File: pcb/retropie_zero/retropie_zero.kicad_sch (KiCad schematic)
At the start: 32 parts, among them J1 Conn_01x02_Socket, J2 Conn_01x10_Pin, SW1 SW_DIP_x01, SW10 SW_DIP_x01, SW11 SW_DIP_x01, SW12 SW_DIP_x01, SW13 SW_DIP_x01, SW14 SW_DIP_x01, SW2 SW_DIP_x01, SW3 SW_DIP_x01, SW4 SW_DIP_x01, SW5 SW_DIP_x01, SW6 SW_DIP_x01, SW7 SW_DIP_x01, SW8 SW_DIP_x01, SW9 SW_DIP_x01, U3 PAM8302AASCR, X1 TERMBLOCK_1X2

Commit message: Fixed some stuff, removed irrelevant reference
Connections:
- net DPAD_D: now also U1.5 (GPIO3)
- net DPAD_L: now also U1.7 (GPIO4)
- net DPAD_R: now also U1.11 (GPIO17)
- net DPAD_U: now also U1.3 (GPIO2)
- net L_BUMP: now also U1.8 (GPIO14)
- net R_BUMP: now also U1.16 (GPIO23)
- net R_TRIG: now also U1.10 (GPIO15), U1.26 (GPIO7)
- net SW_A: now also U1.29 (GPIO5)
- net SW_B: now also U1.15 (GPIO22)
- net SW_SEL: now also U1.31 (GPIO6)
- net SW_STA: now also U1.35 (GPIO19)
- net SW_X: now also U1.13 (GPIO27)
- net SW_Y: now also U1.21 (GPIO9)

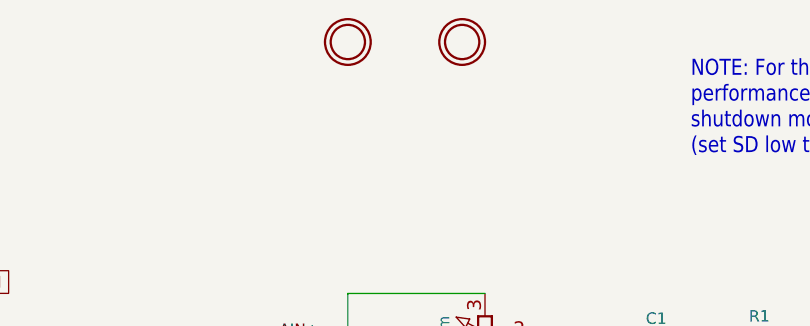
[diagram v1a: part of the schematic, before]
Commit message: Assigned footprints, ignoring backups now
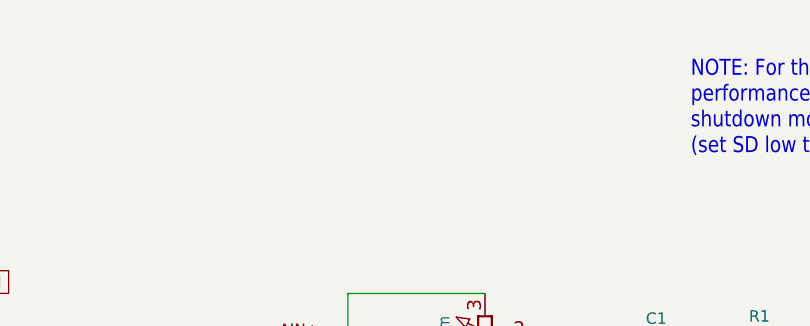
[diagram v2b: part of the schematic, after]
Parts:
- removed U$10, U$11: MOUNTINGHOLE2.0, Adafruit PAM8302:MOUNTINGHOLE_2.0_PLATED, symbol Adafruit PAM8302-eagle-import:MOUNTINGHOLE2.0
- C1, C2, C3, C4, C5: footprint Adafruit PAM8302:0805-NO -> Capacitor_SMD:C_0805_2012Metric_Pad1.18x1.45mm_HandSolder
- FB1, FB2: footprint Adafruit PAM8302:_0805 -> Capacitor_SMD:C_0805_2012Metric
- J1: footprint (none) -> Connector_PinHeader_2.54mm:PinHeader_1x02_P2.54mm_Vertical
- J2: footprint (none) -> Connector_PinHeader_2.54mm:PinHeader_1x10_P2.54mm_Vertical
- R1, R2, R3: footprint Adafruit PAM8302:0805-NO -> Resistor_SMD:R_0805_2012Metric
- SW1, SW10, SW11, SW12, SW13, SW14, SW2, SW3, SW4, SW5, SW6, SW7, SW8, SW9: footprint (none) -> Button_Switch_THT:SW_PUSH_6mm
- U1: footprint (none) -> lib:RPI Zero Footprint
- U3: footprint Adafruit PAM8302:MSOP8_0.65MM -> lib:PAM8302AADCR
- VR1: footprint Adafruit PAM8302:TRIMPOT_BOURNS_3303W -> Potentiometer_THT:Potentiometer_Runtron_RM-065_Vertical
- X1: footprint Adafruit PAM8302:TERMBLOCK_1X2-3.5MM -> TerminalBlock_4Ucon:TerminalBlock_4Ucon_1x02_P3.50mm_Horizontal
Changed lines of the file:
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@@
 			)
 		)
-		(property "Footprint" "Adafruit PAM8302:0805-NO"
+		(property "Footprint" "Capacitor_SMD:C_0805_2012Metric_Pad1.18x1.45mm_HandSolder"
 			(at 241.3 68.58 0)
 			(effects
@@
 			)
 		)
-		(property "Footprint" "Adafruit PAM8302:_0805"
+		(property "Footprint" "Capacitor_SMD:C_0805_2012Metric"
 			(at 228.6 50.8 0)
 			(effects
@@
 			)
 		)
-		(property "Footprint" "Adafruit PAM8302:MSOP8_0.65MM"
+		(property "Footprint" "lib:PAM8302AADCR"
 			(at 210.82 60.96 0)
 			(effects
@@
 			)
 		)
-		(property "Footprint" ""
+		(property "Footprint" "Button_Switch_THT:SW_PUSH_6mm"
 			(at 161.29 152.4 0)
 			(effects
@@
 			)
 		)
-		(property "Footprint" ""
+		(property "Footprint" "Button_Switch_THT:SW_PUSH_6mm"
 			(at 81.28 194.31 0)
 			(effects
@@
 			)
 		)
-		(property "Footprint" "Adafruit PAM8302:0805-NO"
+		(property "Footprint" "Capacitor_SMD:C_0805_2012Metric_Pad1.18x1.45mm_HandSolder"
 			(at 180.34 78.74 0)
 			(effects
@@
 			)
 		)
-		(property "Footprint" ""
+		(property "Footprint" "lib:RPI Zero Footprint"
 			(at 58.42 53.34 0)
 			(effects
@@
 			)
 		)
-		(property "Footprint" ""
+		(property "Footprint" "Connector_PinHeader_2.54mm:PinHeader_1x02_P2.54mm_Vertical"
 			(at 127 60.96 0)
 			(effects
@@
 	)
 	(symbol
-		(lib_id "Adafruit PAM8302-eagle-import:MOUNTINGHOLE2.0")
-		(at 144.78 17.78 0)
-		(unit 1)
-		(exclude_from_sim no)
-		(in_bom yes)
-		(on_board yes)
-		(dnp no)
-		(property "Reference" "U$11"
-			(at 144.78 17.78 0)
-			(effects
-				(font
-					(size 1.27 1.27)
-				)
-				(hide yes)
-			)
-		)
-		(property "Value" "MOUNTINGHOLE2.0"
-			(at 144.78 17.78 0)
-			(effects
-				(font
-					(size 1.27 1.27)
-				)
-				(hide yes)
-			)
-		)
-		(property "Footprint" "Adafruit PAM8302:MOUNTINGHOLE_2.0_PLATED"
-			(at 144.78 17.78 0)
-			(effects
-				(font
-					(size 1.27 1.27)
-				)
-				(hide yes)
-			)
-		)
-		(property "Datasheet" ""
-			(at 144.78 17.78 0)
-			(effects
-				(font
-					(size 1.27 1.27)
-				)
-				(hide yes)
-			)
-		)
-		(property "Description" ""
-			(at 144.78 17.78 0)
-			(effects
-				(font
-					(size 1.27 1.27)
-				)
-				(hide yes)
-			)
-		)
-		(instances
-			(project "retropie_zero"
-				(path "/f5395351-1217-49d5-a52e-3316d9db527f"
-					(reference "U$11")
-					(unit 1)
-				)
-			)
-		)
-	)
-	(symbol
 		(lib_id "Switch:SW_DIP_x01")
 		(at 181.61 152.4 0)
@@
 			)
 		)
-		(property "Footprint" ""
+		(property "Footprint" "Button_Switch_THT:SW_PUSH_6mm"
 			(at 181.61 152.4 0)
 			(effects
@@
 			)
 		)
-		(property "Footprint" "Adafruit PAM8302:0805-NO"
+		(property "Footprint" "Capacitor_SMD:C_0805_2012Metric_Pad1.18x1.45mm_HandSolder"
 			(at 177.8 50.8 0)
 			(effects
@@
 			)
 		)
-		(property "Footprint" ""
+		(property "Footprint" "Button_Switch_THT:SW_PUSH_6mm"
 			(at 194.31 195.58 0)
 			(effects
@@
 			)
 		)
-		(property "Footprint" ""
+		(property "Footprint" "Button_Switch_THT:SW_PUSH_6mm"
 			(at 148.59 195.58 0)
 			(effects
@@
 			)
 		)
-		(property "Footprint" ""
+		(property "Footprint" "Button_Switch_THT:SW_PUSH_6mm"
 			(at 77.47 152.4 0)
 			(effects
@@
 			)
 		)
-		(property "Footprint" "Adafruit PAM8302:TERMBLOCK_1X2-3.5MM"
+		(property "Footprint" "TerminalBlock_4Ucon:TerminalBlock_4Ucon_1x02_P3.50mm_Horizontal"
 			(at 261.62 55.88 0)
 			(effects
@@
 			)
 		)
-		(property "Footprint" ""
+		(property "Footprint" "Button_Switch_THT:SW_PUSH_6mm"
 			(at 57.15 214.63 0)
 			(effects
@@
 			)
 		)
-		(property "Footprint" "Adafruit PAM8302:0805-NO"
+		(property "Footprint" "Capacitor_SMD:C_0805_2012Metric_Pad1.18x1.45mm_HandSolder"
 			(at 233.68 68.58 0)
 			(effects
@@
 			)
 		)
-		(property "Footprint" ""
+		(property "Footprint" "Button_Switch_THT:SW_PUSH_6mm"
 			(at 170.18 181.61 0)
 			(effects
@@
 			)
 		)
-		(property "Footprint" "Adafruit PAM8302:0805-NO"
+		(property "Footprint" "Resistor_SMD:R_0805_2012Metric"
 			(at 190.5 60.96 0)
 			(effects
@@
 			)
 		)
-		(property "Footprint" ""
+		(property "Footprint" "Button_Switch_THT:SW_PUSH_6mm"
 			(at 35.56 194.31 0)
 			(effects
@@
 			)
 		)
-		(property "Footprint" "Adafruit PAM8302:0805-NO"
+		(property "Footprint" "Capacitor_SMD:C_0805_2012Metric_Pad1.18x1.45mm_HandSolder"
 			(at 177.8 60.96 0)
 			(effects
@@
 			)
 		)
-		(property "Footprint" ""
+		(property "Footprint" "Button_Switch_THT:SW_PUSH_6mm"
 			(at 102.87 222.25 0)
 			(effects
@@
 			)
 		)
-		(property "Footprint" ""
+		(property "Footprint" "Button_Switch_THT:SW_PUSH_6mm"
 			(at 57.15 152.4 0)
 			(effects
@@
 			)
 		)
-		(property "Footprint" "Adafruit PAM8302:0805-NO"
+		(property "Footprint" "Resistor_SMD:R_0805_2012Metric"
 			(at 190.5 50.8 0)
 			(effects
@@
 			)
 		)
-		(property "Footprint" ""
+		(property "Footprint" "Button_Switch_THT:SW_PUSH_6mm"
 			(at 170.18 215.9 0)
 			(effects
@@
 			)
 		)
-		(property "Footprint" ""
+		(property "Footprint" "Button_Switch_THT:SW_PUSH_6mm"
 			(at 123.19 222.25 0)
 			(effects
@@
 			)
 		)
-		(property "Footprint" ""
+		(property "Footprint" "Button_Switch_THT:SW_PUSH_6mm"
 			(at 57.15 180.34 0)
 			(effects
@@
 			)
 		)
-		(property "Footprint" "Adafruit PAM8302:TRIMPOT_BOURNS_3303W"
+		(property "Footprint" "Potentiometer_THT:Potentiometer_Runtron_RM-065_Vertical"
 			(at 160.02 50.8 0)
 			(effects
@@
 	)
 	(symbol
-		(lib_id "Adafruit PAM8302-eagle-import:MOUNTINGHOLE2.0")
-		(at 157.48 17.78 0)
-		(unit 1)
-		(exclude_from_sim no)
-		(in_bom yes)
-		(on_board yes)
-		(dnp no)
-		(property "Reference" "U$10"
-			(at 157.48 17.78 0)
-			(effects
-				(font
-					(size 1.27 1.27)
-				)
-				(hide yes)
-			)
-		)
-		(property "Value" "MOUNTINGHOLE2.0"
-			(at 157.48 17.78 0)
-			(effects
-				(font
-					(size 1.27 1.27)
-				)
-				(hide yes)
-			)
-		)
-		(property "Footprint" "Adafruit PAM8302:MOUNTINGHOLE_2.0_PLATED"
-			(at 157.48 17.78 0)
-			(effects
-				(font
-					(size 1.27 1.27)
-				)
-				(hide yes)
-			)
-		)
-		(property "Datasheet" ""
-			(at 157.48 17.78 0)
-			(effects
-				(font
-					(size 1.27 1.27)
-				)
-				(hide yes)
-			)
-		)
-		(property "Description" ""
-			(at 157.48 17.78 0)
-			(effects
-				(font
-					(size 1.27 1.27)
-				)
-				(hide yes)
-			)
-		)
-		(instances
-			(project "retropie_zero"
-				(path "/f5395351-1217-49d5-a52e-3316d9db527f"
-					(reference "U$10")
-					(unit 1)
-				)
-			)
-		)
-	)
-	(symbol
 		(lib_id "power:GND")
 		(at 69.85 152.4 0)
@@
 			)
 		)
-		(property "Footprint" "Adafruit PAM8302:0805-NO"
+		(property "Footprint" "Resistor_SMD:R_0805_2012Metric"
 			(at 187.96 66.04 0)
 			(effects
@@
 			)
 		)
-		(property "Footprint" ""
+		(property "Footprint" "Connector_PinHeader_2.54mm:PinHeader_1x10_P2.54mm_Vertical"
 			(at 104.14 104.14 0)
 			(effects
@@
 			)
 		)
-		(property "Footprint" "Adafruit PAM8302:_0805"
+		(property "Footprint" "Capacitor_SMD:C_0805_2012Metric"
 			(at 228.6 60.96 0)
 			(effects

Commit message: PCB Routing finished
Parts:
- added SPC1, SPC2: Button Spacer, lib:button_spacer, symbol Connector:Conn_01x01_Pin
- added X2: TERMBLOCK_1X2, TerminalBlock_4Ucon:TerminalBlock_4Ucon_1x02_P3.50mm_Horizontal, symbol Adafruit PAM8302-eagle-import:TERMBLOCK_1X2
- SW10, SW11, SW12, SW9: footprint Button_Switch_THT:SW_PUSH_6mm -> Connector_PinHeader_2.54mm:PinHeader_1x02_P2.54mm_Vertical
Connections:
- net GND: now also X2.2
- net PowerBoost Power: now also X2.1
- no-connect marks 3 -> 14

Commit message: Wiring finished
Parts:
- removed SPC1, SPC2: Button Spacer, lib:button_spacer, symbol Connector:Conn_01x01_Pin
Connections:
- net R_TRIG: no longer SW10.2, U1.10 (GPIO15)
- new net L_TRIG: SW10.2, U1.10 (GPIO15)
- no-connect marks 14 -> 12
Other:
- note added: "Assembly Note: The button labels are flipped. This means that the buttons labeled "DPAD" are actually the buttonpad, and vice versa."
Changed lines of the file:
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@@
 	(generator_version "9.0")
 	(paper "A2")
+	(text "Assembly\nNote: The button labels are flipped. This means that the buttons labeled \"DPAD\" are actually the buttonpad, and vice versa."
+		(exclude_from_sim no)
+		(at 161.544 121.92 0)
+		(effects
+			(font
+				(size 2.54 2.54)
+			)
+		)
+	)
 	(text "NOTE: For the best power on/off pop\nperformance, the amplifier should be set in the\nshutdown mode prior to power on/off operation\n(set SD low to power down the amp)."
 		(exclude_from_sim no)
@@
 	)
 	(no_connect
-		(at 234.95 205.74)
-	)
-	(no_connect
-		(at 238.76 218.44)
-	)
-	(no_connect
 		(at 72.39 86.36)
 	)
@@
 		)
 	)
-	(global_label "R_TRIG"
+	(global_label "L_TRIG"
 		(shape input)
 		(at 85.09 142.24 90)
@@
 		)
 		(property "Intersheetrefs" "${INTERSHEET_REFS}"
-			(at 85.09 132.9048 90)
+			(at 85.09 133.1467 90)
 			(effects
 				(font
@@
 		)
 	)
-	(global_label "R_TRIG"
+	(global_label "L_TRIG"
 		(shape input)
 		(at 72.39 52.07 0)
@@
 		)
 		(property "Intersheetrefs" "${INTERSHEET_REFS}"
-			(at 81.7252 52.07 0)
+			(at 81.4833 52.07 0)
 			(effects
 				(font
@@
 	)
 	(symbol
-		(lib_id "Connector:Conn_01x01_Pin")
-		(at 233.68 218.44 0)
-		(unit 1)
-		(exclude_from_sim no)
-		(in_bom yes)
-		(on_board yes)
-		(dnp no)
-		(fields_autoplaced yes)
-		(property "Reference" "SPC2"
-			(at 234.315 213.36 0)
-			(effects
-				(font
-					(size 1.27 1.27)
-				)
-			)
-		)
-		(property "Value" "Button Spacer"
-			(at 234.315 215.9 0)
-			(effects
-				(font
-					(size 1.27 1.27)
-				)
-			)
-		)
-		(property "Footprint" "lib:button_spacer"
-			(at 233.68 218.44 0)
-			(effects
-				(font
-					(size 1.27 1.27)
-				)
-				(hide yes)
-			)
-		)
-		(property "Datasheet" "~"
-			(at 233.68 218.44 0)
-			(effects
-				(font
-					(size 1.27 1.27)
-				)
-				(hide yes)
-			)
-		)
-		(property "Description" "Generic connector, single row, 01x01, script generated"
-			(at 233.68 218.44 0)
-			(effects
-				(font
-					(size 1.27 1.27)
-				)
-				(hide yes)
-			)
-		)
-		(pin "1"
-		)
-		(instances
-			(project "retropie_zero"
-				(path "/f5395351-1217-49d5-a52e-3316d9db527f"
-					(reference "SPC2")
-					(unit 1)
-				)
-			)
-		)
-	)
-	(symbol
 		(lib_id "Adafruit PAM8302-eagle-import:GND")
 		(at 195.58 86.36 0)
@@
 					(unit 1)
 				)
-			)
-		)
-	)
-	(symbol
-		(lib_id "Connector:Conn_01x01_Pin")
-		(at 229.87 205.74 0)
-		(unit 1)
-		(exclude_from_sim no)
-		(in_bom yes)
-		(on_board yes)
-		(dnp no)
-		(fields_autoplaced yes)
-		(property "Reference" "SPC1"
-			(at 230.505 200.66 0)
-			(effects
-				(font
-					(size 1.27 1.27)
-				)
-			)
-		)
-		(property "Value" "Button Spacer"
-			(at 230.505 203.2 0)
-			(effects
-				(font
-					(size 1.27 1.27)
-				)
-			)
-		)
-		(property "Footprint" "lib:button_spacer"
-			(at 229.87 205.74 0)
-			(effects
-				(font
-					(size 1.27 1.27)
-				)
-				(hide yes)
-			)
-		)
-		(property "Datasheet" "~"
-			(at 229.87 205.74 0)
-			(effects
-				(font
-					(size 1.27 1.27)
-				)
-				(hide yes)
-			)
-		)
-		(property "Description" "Generic connector, single row, 01x01, script generated"
-			(at 229.87 205.74 0)
-			(effects
-				(font
-					(size 1.27 1.27)
-				)
-				(hide yes)
-			)
-		)
-		(pin "1"
-		)
-		(instances
-			(project ""
-				(path "/f5395351-1217-49d5-a52e-3316d9db527f"
-					(reference "SPC1")
-					(unit 1)
-				)

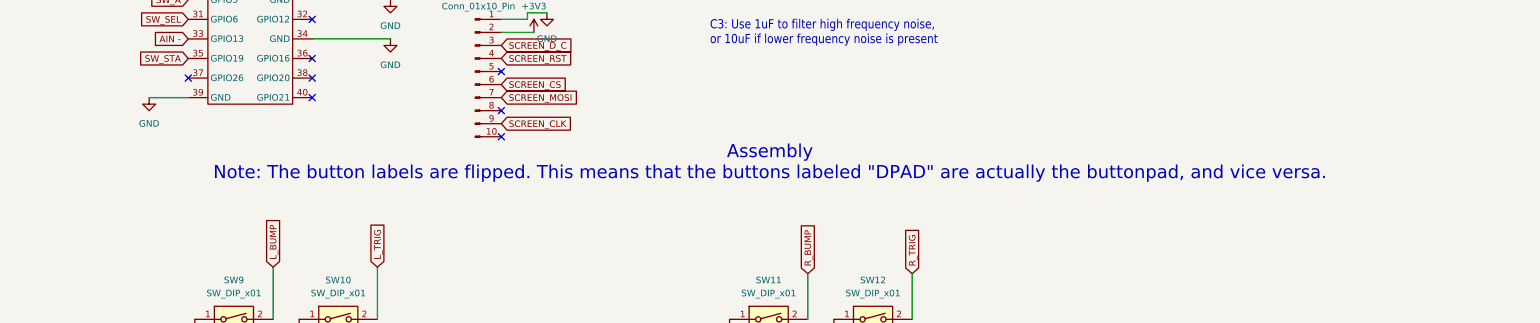
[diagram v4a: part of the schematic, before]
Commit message: Board Outline Fixed
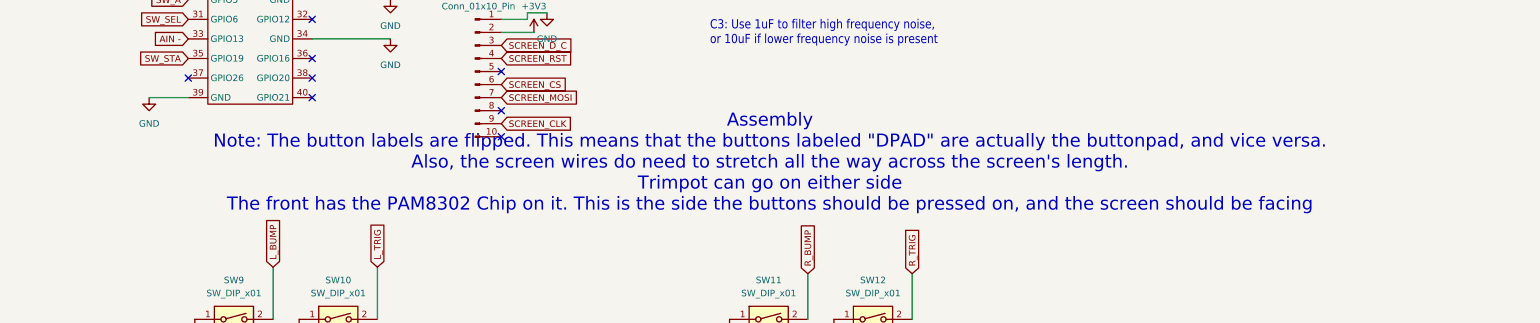
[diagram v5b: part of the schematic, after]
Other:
- note added: "Assembly Note: The button labels are flipped. This means that the buttons labeled "DPAD" are actually the buttonpad, and vice versa. Also, the screen wires do need to stretch all the way across the screen's length. Trimpot can go on either side The front has the PAM8302 Chip on it. This is the side the buttons should be pressed on, and the screen should be facing"
- note removed: "Assembly Note: The button labels are flipped. This means that the buttons labeled "DPAD" are actually the buttonpad, and vice versa."
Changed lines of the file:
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@@
 	(generator_version "9.0")
 	(paper "A2")
-	(text "Assembly\nNote: The button labels are flipped. This means that the buttons labeled \"DPAD\" are actually the buttonpad, and vice versa."
+	(text "Assembly\nNote: The button labels are flipped. This means that the buttons labeled \"DPAD\" are actually the buttonpad, and vice versa.\nAlso, the screen wires do need to stretch all the way across the screen's length.\nTrimpot can go on either side\nThe front has the PAM8302 Chip on it. This is the side the buttons should be pressed on, and the screen should be facing"
 		(exclude_from_sim no)
 		(at 161.544 121.92 0)
